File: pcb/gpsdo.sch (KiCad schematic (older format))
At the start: 148 parts, among them IC1 ICE40LP384-SG32, J1 JTAG, J10 CLK0, J11 USB_B_Micro, J12 CLK7, J13 CLK6, J14 CLK5, J15 CLK4, J2 EXT_CLOCK, J3 SSD1306, J4 USB_B_Micro, J5 GPS_ANT, J6 CLK3, J7 Screw_Terminal_01x03, J8 CLK2, J9 CLK1, M1 E73-2G4M08S1C-52840, Q1 S9018, SW1 EC11, SW2 MCML4-112B, U1 Si7020-A20, U2 TPS652510, U3 LT1763xS8, U4 74LVC1G17, U5 Si5351C-B-GM, U6 74LVC1G17, U7 uBlox NEO-7M, U8 AD5761R, Y1 32768, Y2 8663-XS

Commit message: first routing tests
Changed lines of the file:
@@
 	8150 4150 8150 4200
 Wire Wire Line
+	8750 3650 8750 4200
+Wire Wire Line
 	7550 3650 7550 4200
-Wire Wire Line
-	8750 3650 8750 4200
+Text Label 7550 4200 1    50   ~ 0
+GPS_USB_D+
 Text Label 8750 4200 1    50   ~ 0
-GPS_USB_D+
-Text Label 7550 4200 1    50   ~ 0
 GPS_USB_D-
 $Comp

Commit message: replace expensive Si7010 with two cheaper temp sensors
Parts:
- removed U1: Si7020-A20, Package_DFN_QFN:DFN-6-1EP_3x3mm_P1mm_EP1.5x2.4mm, symbol Sensor_Humidity:Si7020-A20
- added C1: 100n, Capacitor_SMD:C_0402_1005Metric, symbol Device:C
- added R10: 10K, Resistor_SMD:R_0402_1005Metric, symbol Device:R
- added U1, U2: MCP9808_MSOP, Package_SO:MSOP-8_3x3mm_P0.65mm, symbol Sensor_Temperature:MCP9804_MSOP
- renumbered C9 to C10, C10 to C12, C12 to C13, C13 to C14, C14 to C15, C15 to C16, C16 to C17, C17 to C18, C18 to C19, C1 to C2, C19 to C20, C22 to C21, C20 to C22, C24 to C23, C25 to C24, C26 to C25, C21 to C26, C23 to C27, C27 to C29, C2 to C3, C29 to C31, C31 to C32, C32 to C33, C33 to C34, C34 to C35, C35 to C36, C36 to C37, C37 to C38, C38 to C39, C3 to C4, C39 to C40, C40 to C41, C41 to C42, C42 to C43, C43 to C44, C44 to C45, C45 to C46, C46 to C47, C47 to C48, C4 to C5, C5 to C6, C6 to C7, C7 to C8, C8 to C9, J12 to J11, J11 to J12, J3 to J2, J2 to J3, J5 to J4, J4 to J5, R2 to R1, R12 to R11, R13 to R12, R14 to R13, R15 to R14, R1 to R15, R9 to R16, R16 to R17, R17 to R18, R18 to R19, R3 to R2, R19 to R20, R20 to R21, R21 to R22, R22 to R23, R23 to R27, R4 to R3, R27 to R30, R30 to R31, R31 to R32, R32 to R33, R33 to R34, R34 to R35, R35 to R36, R36 to R37, R37 to R38, R38 to R39, R5 to R4, R39 to R40, R40 to R41, R41 to R42, R42 to R43, R43 to R44, R44 to R45, R45 to R46, R46 to R47, R47 to R48, R48 to R49, R6 to R5, R7 to R6, R8 to R7, R10 to R8, R11 to R9, U2 to U3, U3 to U4, U4 to U5, U5 to U6, U6 to U7, U7 to U8, U8 to U9
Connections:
- net labels added: TEMP_ALERT
- net labels removed: EN_10V_PU
- wire segments 663 -> 687
- no-connect marks 18 -> 16
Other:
- note added: "i2c Address 0x18"
- note added: "i2c Address 0x19"
- note removed: "i2c Address 0x40"
- moved on the sheet: C10, C11, C12, C13, C14, C15, C16, C17, C18, C19, C2, C20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

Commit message: tps652510 routing, inductor footprint
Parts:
- L1, L2, L3: footprint Inductor_SMD:L_2816_7142Metric -> Inductor_SMD:L_Wuerth_HCI-7050
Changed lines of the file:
@@
 F 0 "L3" V 5050 2500 50  0000 C CNN
 F 1 "4u7" V 5050 2700 50  0000 C CNN
-F 2 "Inductor_SMD:L_2816_7142Metric" H 5100 2600 50  0001 C CNN
+F 2 "Inductor_SMD:L_Wuerth_HCI-7050" H 5100 2600 50  0001 C CNN
 F 3 "~" H 5100 2600 50  0001 C CNN
 	1    5100 2600
@@
 F 0 "L2" V 5050 1900 50  0000 C CNN
 F 1 "4u7" V 5050 2100 50  0000 C CNN
-F 2 "Inductor_SMD:L_2816_7142Metric" H 5100 2000 50  0001 C CNN
+F 2 "Inductor_SMD:L_Wuerth_HCI-7050" H 5100 2000 50  0001 C CNN
 F 3 "~" H 5100 2000 50  0001 C CNN
 	1    5100 2000
@@
 F 0 "L1" V 5050 1300 50  0000 C CNN
 F 1 "4u7" V 5050 1500 50  0000 C CNN
-F 2 "Inductor_SMD:L_2816_7142Metric" H 5100 1400 50  0001 C CNN
+F 2 "Inductor_SMD:L_Wuerth_HCI-7050" H 5100 1400 50  0001 C CNN
 F 3 "~" H 5100 1400 50  0001 C CNN
 	1    5100 1400

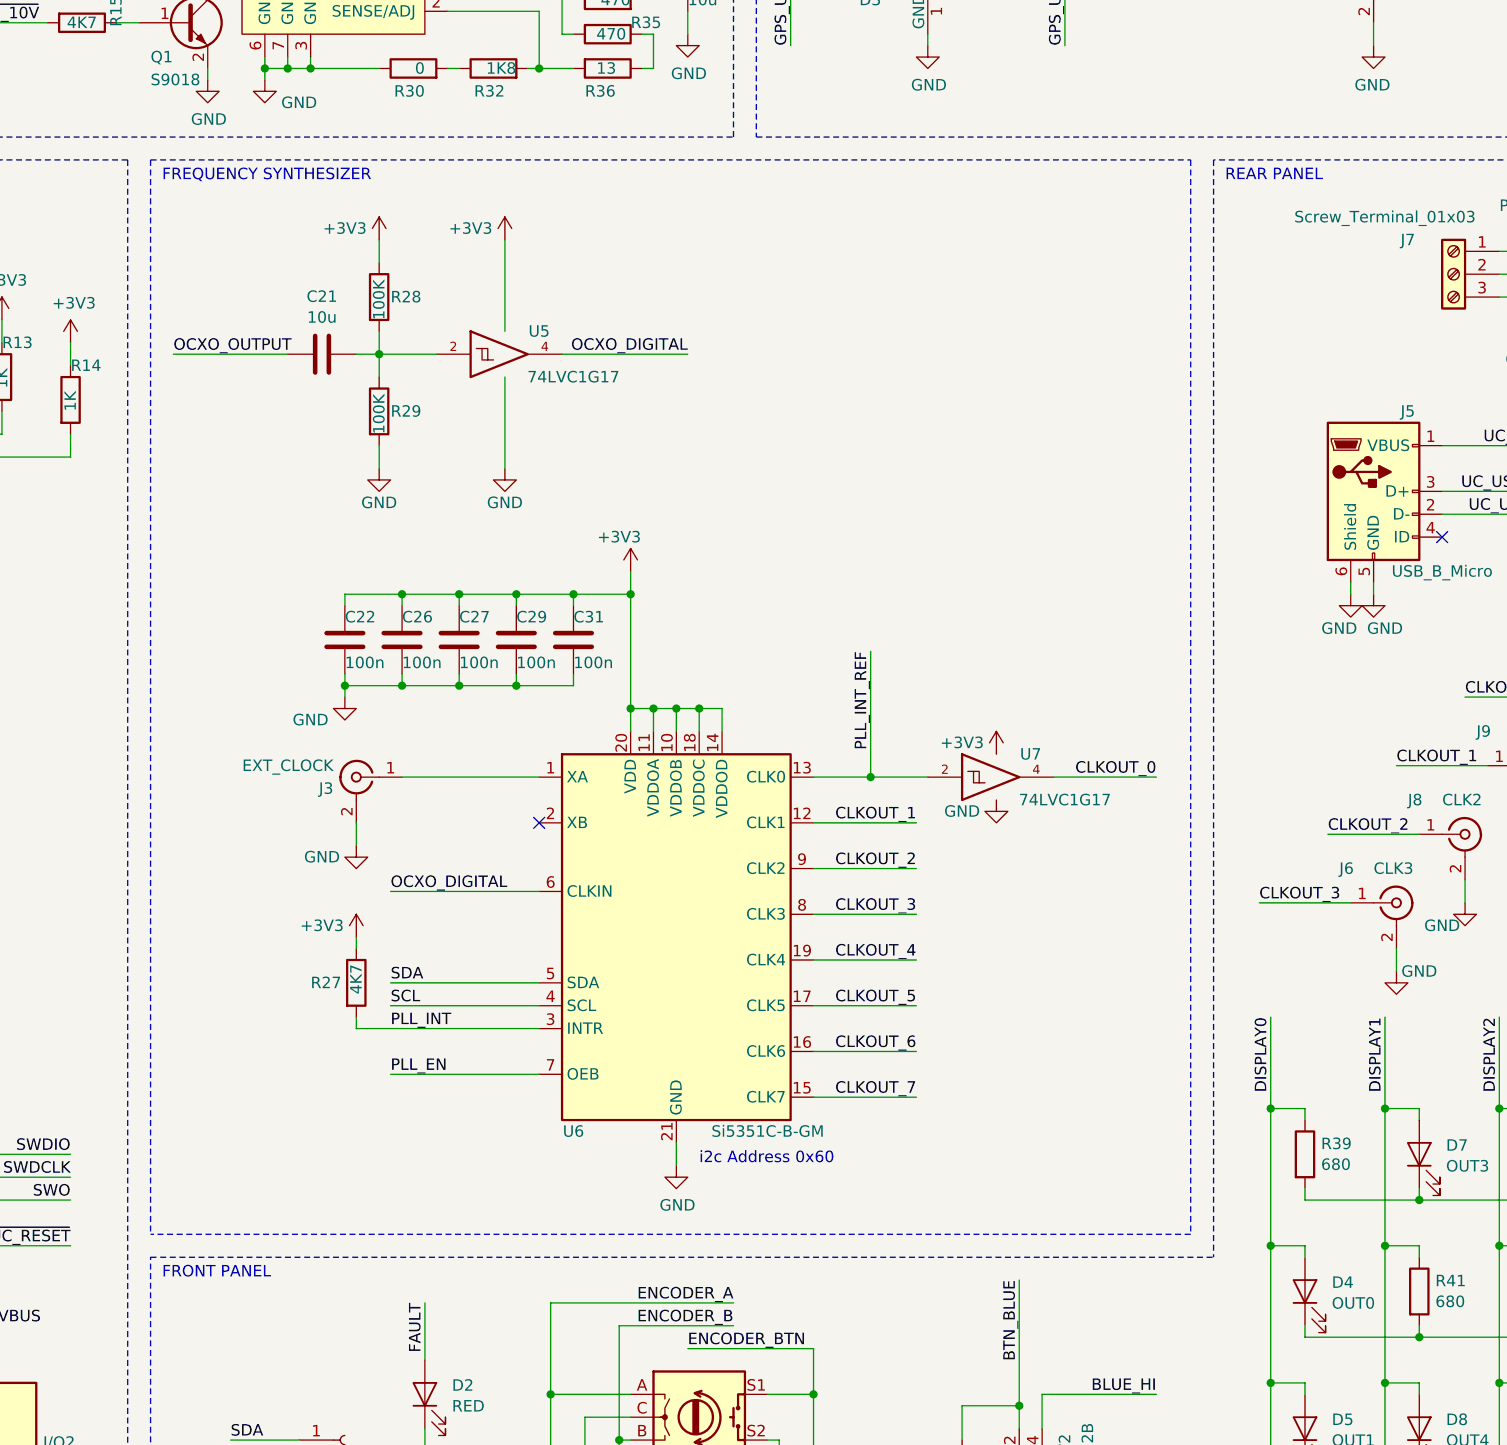
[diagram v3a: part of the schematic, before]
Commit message: basic component placement and board layout
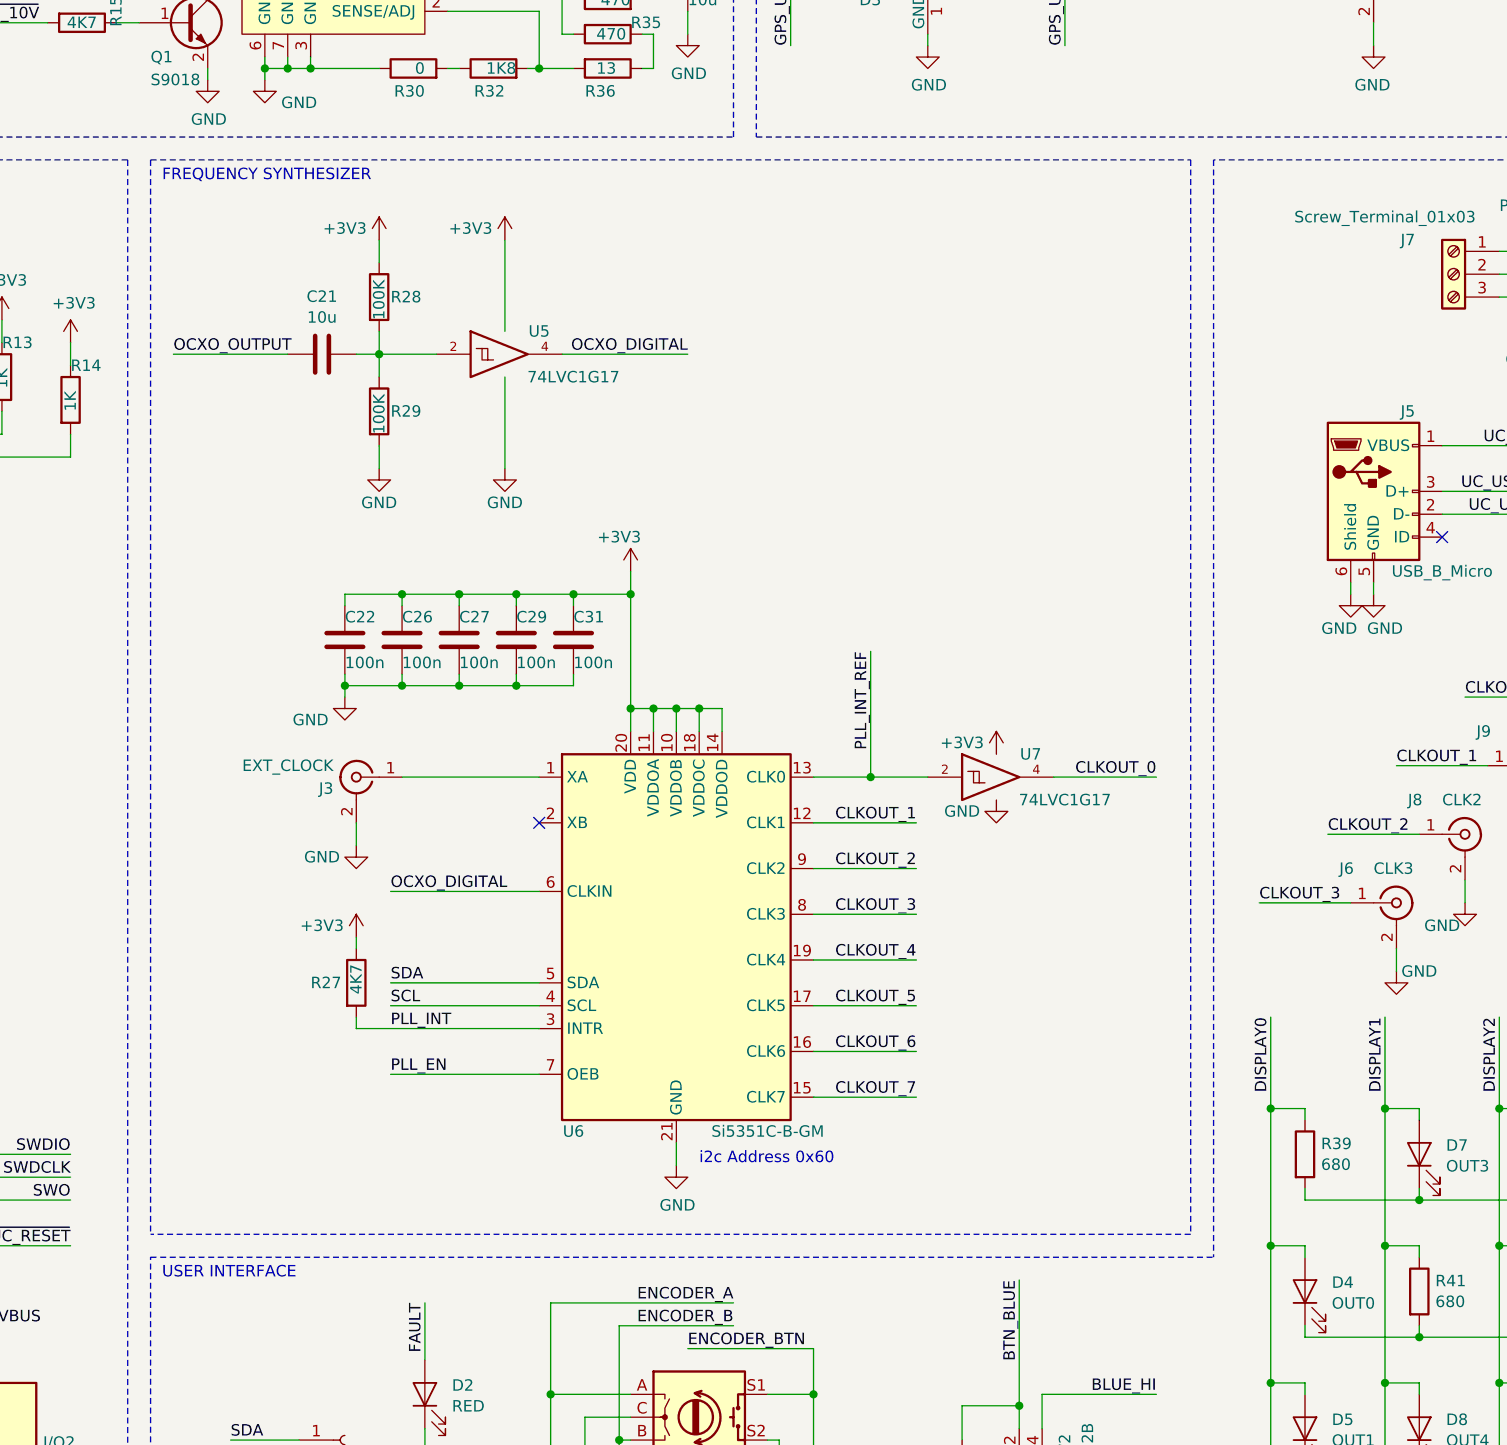
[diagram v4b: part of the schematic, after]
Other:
- note added: "USER INTERFACE"
- note removed: "FRONT PANEL"
- note removed: "REAR PANEL"
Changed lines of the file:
@@
 	4750 11150 4750 9500
 Text Notes 4800 9600 0    50   ~ 0
-FRONT PANEL
+USER INTERFACE
 Wire Wire Line
 	700  7300 1200 7300
@@
 Wire Notes Line
 	12600 4700 12600 9900
-Text Notes 9450 4800 0    50   ~ 0
-REAR PANEL
 Wire Wire Line
 	6850 6500 6850 6600

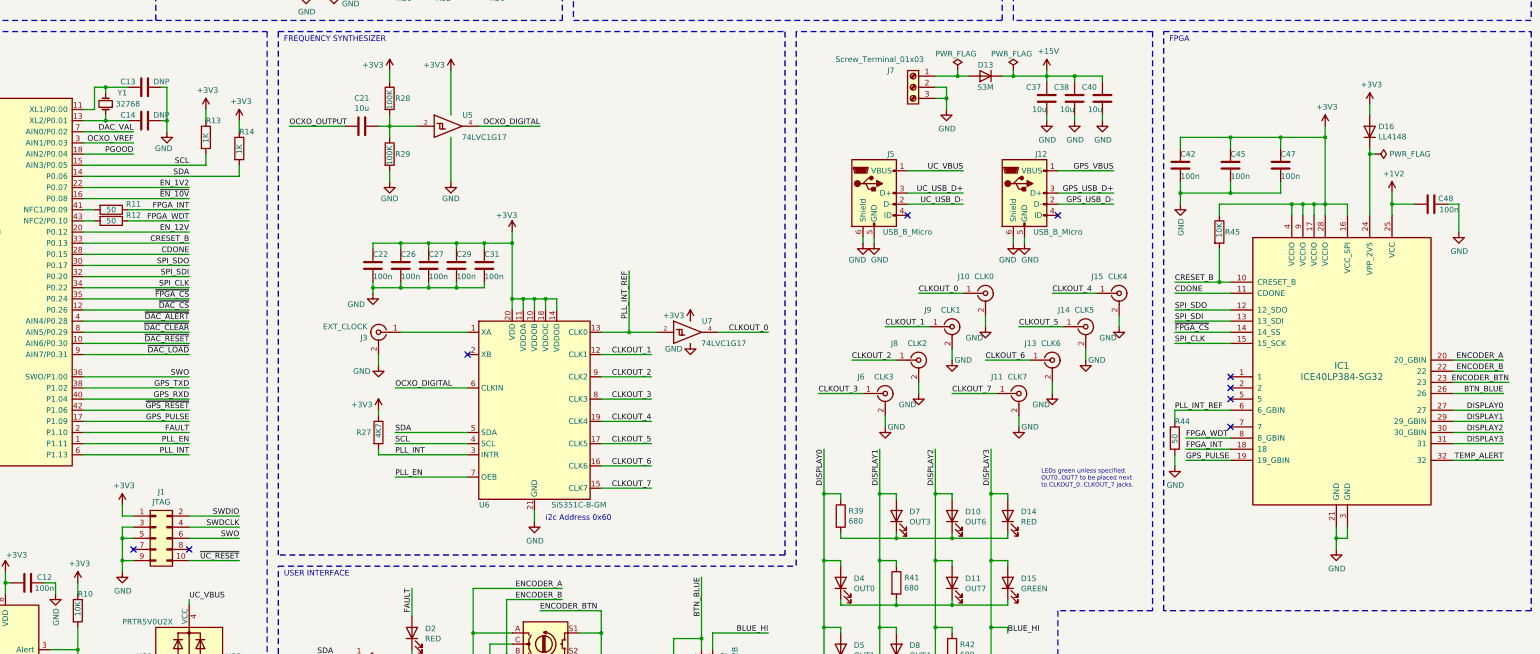
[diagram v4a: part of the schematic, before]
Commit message: pin assignment optimization, routing
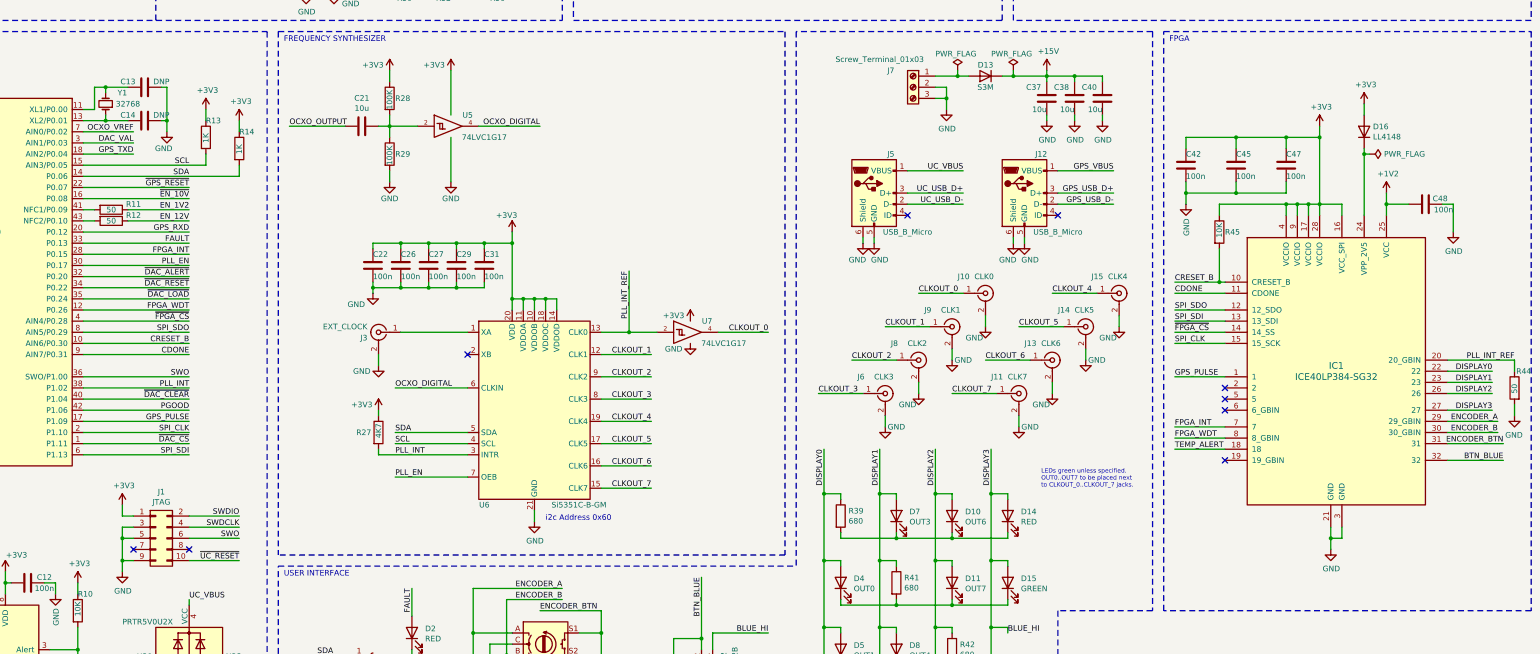
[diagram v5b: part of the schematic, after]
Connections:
- net BLUE_HI: now also IC1.27; no longer IC1.31
- net BTN_BLUE: now also IC1.32; no longer IC1.26
- net CDONE: now also M1.9 (AIN7/P0.31); no longer M1.28 (P0.15)
- net CRESET_B: now also M1.10 (AIN6/P0.30); no longer M1.33 (P0.13)
- net DAC_VAL: now also M1.3 (AIN1/P0.03); no longer M1.7 (AIN0/P0.02)
- net DISPLAY0: now also IC1.22; no longer IC1.27
- net DISPLAY1: now also IC1.23; no longer IC1.29 (29_GBIN)
- net DISPLAY2: now also IC1.26; no longer IC1.30 (30_GBIN)
- net ENCODER_A: now also IC1.29 (29_GBIN); no longer IC1.20 (20_GBIN)
- net ENCODER_B: now also IC1.30 (30_GBIN); no longer IC1.22
- net ENCODER_BTN: now also IC1.31; no longer IC1.23
- net EN_12V: now also R12.1; no longer M1.20 (P0.12)
- net EN_1V2: now also R11.1; no longer M1.22 (P0.07)
- net FAULT: now also M1.33 (P0.13); no longer M1.2 (P1.10)
- net FPGA_INT: now also IC1.7, M1.28 (P0.15); no longer IC1.18, R11.1
- net FPGA_WDT: now also M1.12 (P0.26); no longer R12.1
- net GPS_PULSE: now also IC1.1; no longer IC1.19 (19_GBIN)
- net GPS_RXD: now also M1.20 (P0.12); no longer M1.40 (P1.04)
- net GPS_TXD: now also M1.18 (AIN2/P0.04); no longer M1.38 (P1.02)
- net OCXO_VREF: now also M1.7 (AIN0/P0.02); no longer M1.3 (AIN1/P0.03)
- net PGOOD: now also M1.42 (P1.06); no longer M1.18 (AIN2/P0.04)
- net PLL_EN: now also M1.30 (P0.17); no longer M1.1 (P1.11)
- net PLL_INT: now also M1.38 (P1.02); no longer M1.6 (P1.13)
- net PLL_INT_REF: now also IC1.20 (20_GBIN); no longer IC1.6 (6_GBIN)
- net SPI_CLK: now also M1.2 (P1.10); no longer M1.34 (P0.22)
- net SPI_SDI: now also M1.6 (P1.13); no longer M1.32 (P0.20)
- net SPI_SDO: now also M1.8 (AIN5/P0.29); no longer M1.30 (P0.17)
- net TEMP_ALERT: now also IC1.18; no longer IC1.32
- net ~DAC_ALERT: now also M1.32 (P0.20); no longer M1.4 (AIN4/P0.28)
- net ~DAC_CLEAR: now also M1.40 (P1.04); no longer M1.8 (AIN5/P0.29)
- net ~DAC_CS: now also M1.1 (P1.11); no longer M1.12 (P0.26)
- net ~DAC_LOAD: now also M1.35 (P0.24); no longer M1.9 (AIN7/P0.31)
- net ~DAC_RESET: now also M1.34 (P0.22); no longer M1.10 (AIN6/P0.30)
- net ~FPGA_CS: now also M1.4 (AIN4/P0.28); no longer M1.35 (P0.24)
- net ~GPS_RESET: now also M1.22 (P0.07); no longer M1.42 (P1.06)
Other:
- moved on the sheet: C42, C45, C47, C48, D16, IC1, R44

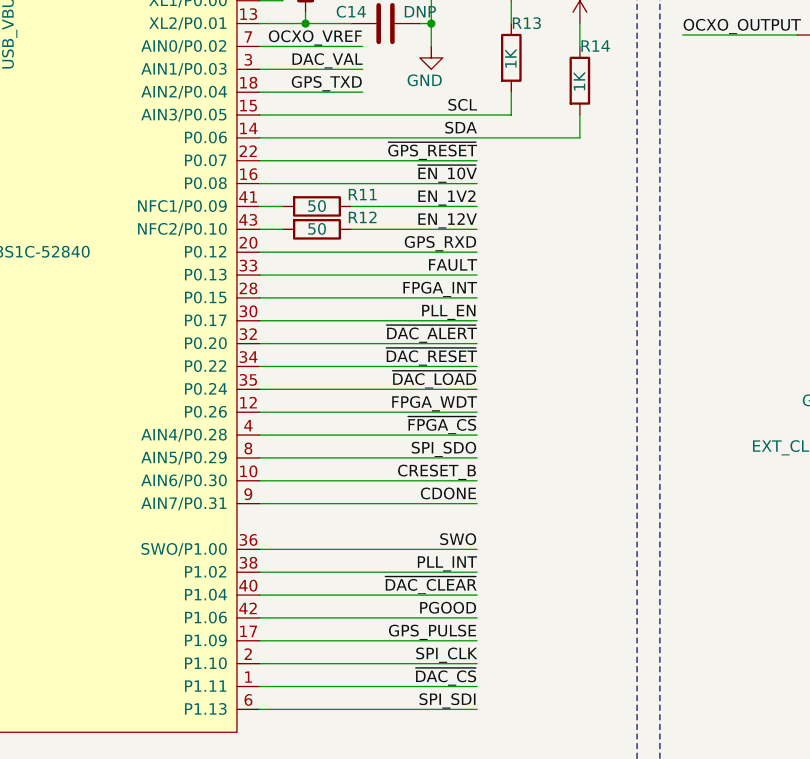
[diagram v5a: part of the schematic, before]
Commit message: pin assignment optimization, routing
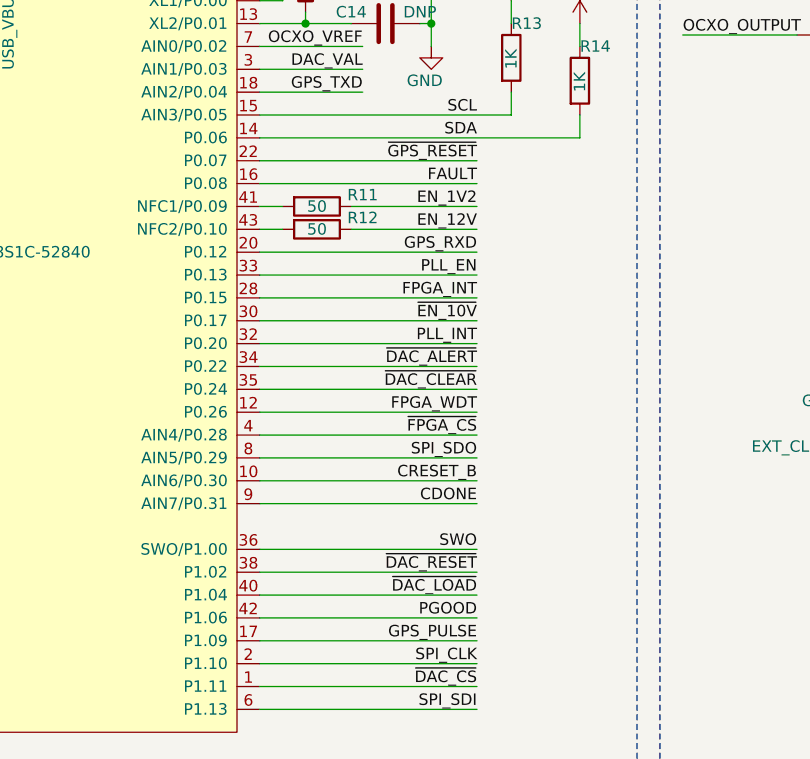
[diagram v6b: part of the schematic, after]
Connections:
- net FAULT: now also M1.16 (P0.08); no longer M1.33 (P0.13)
- net PLL_EN: now also M1.33 (P0.13); no longer M1.30 (P0.17)
- net PLL_INT: now also M1.32 (P0.20); no longer M1.38 (P1.02)
- net ~DAC_ALERT: now also M1.34 (P0.22); no longer M1.32 (P0.20)
- net ~DAC_CLEAR: now also M1.35 (P0.24); no longer M1.40 (P1.04)
- net ~DAC_LOAD: now also M1.40 (P1.04); no longer M1.35 (P0.24)
- net ~DAC_RESET: now also M1.38 (P1.02); no longer M1.34 (P0.22)
- net ~EN_10V: now also M1.30 (P0.17); no longer M1.16 (P0.08)
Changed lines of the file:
@@
 Wire Wire Line
 	3000 8500 3950 8500
-Text Label 3950 7900 2    50   ~ 0
+Text Label 3950 6900 2    50   ~ 0
 PLL_INT
 Wire Wire Line
 	3950 8400 3000 8400
-Text Label 3950 6800 2    50   ~ 0
+Text Label 3950 6600 2    50   ~ 0
 PLL_EN
 Text Label 3950 6500 2    50   ~ 0
@@
 Wire Wire Line
 	3000 7800 3950 7800
+Text Label 3950 8000 2    50   ~ 0
+~DAC_LOAD
+Text Label 3950 7900 2    50   ~ 0
+~DAC_RESET
 Text Label 3950 7100 2    50   ~ 0
-~DAC_LOAD
+~DAC_CLEAR
+Wire Wire Line
+	3950 7600 3000 7600
+Wire Wire Line
+	3000 7500 3950 7500
+Wire Wire Line
+	3950 7400 3000 7400
 Text Label 3950 7000 2    50   ~ 0
-~DAC_RESET
-Text Label 3950 8000 2    50   ~ 0
-~DAC_CLEAR
-Wire Wire Line
-	3950 7600 3000 7600
-Wire Wire Line
-	3000 7500 3950 7500
-Wire Wire Line
-	3950 7400 3000 7400
-Text Label 3950 6900 2    50   ~ 0
 ~DAC_ALERT
 Wire Wire Line
@@
 Text Label 5950 9700 3    50   ~ 0
 FAULT
-Text Label 3950 6600 2    50   ~ 0
+Text Label 3950 6200 2    50   ~ 0
 FAULT
 Wire Wire Line
@@
 Text Label 3950 6300 2    50   ~ 0
 EN_1V2
-Text Label 3950 6200 2    50   ~ 0
+Text Label 3950 6800 2    50   ~ 0
 ~EN_10V
 Wire Wire Line
